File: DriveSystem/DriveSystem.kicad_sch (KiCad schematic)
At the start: 14 parts, among them SW1 SW_Push, SW2 SW_Push, SW3 SW_Push, SW4 SW_Push

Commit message: MC Custom Symbol
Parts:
- removed A1: Arduino_UNO_R2, Module:Arduino_UNO_R2, symbol MCU_Module:Arduino_UNO_R2
- removed RSP1: RSP-750-24, symbol CustomSymbols:RSP-750-24
- added J1: Raspberry_Pi_2_3, symbol Connector:Raspberry_Pi_2_3
- added U1: ~, symbol CustomSymbols:RoboClaw_2x30A_MC
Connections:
- new net: J1.1 (3V3), J1.17 (3V3)
- new net: J1.14 (GND), J1.20 (GND), J1.25 (GND), J1.30 (GND), J1.34 (GND), J1.39 (GND), J1.6 (GND), J1.9 (GND)
- new net: J1.2 (5V), J1.4 (5V)
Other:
- company: (none) -> TERRIER RIDE ENGINEERING CLUB
- title: (none) -> REC 2025 ELECTRONIC SCHEMATIC

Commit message: Merged RCP Schematic
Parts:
- removed C1, C2, C3, C4: 100n, symbol Device:C
- removed J1: Raspberry_Pi_2_3, symbol Connector:Raspberry_Pi_2_3
- removed R1, R2, R3, R4: 1k, symbol Device:R
- removed SW1, SW2, SW3, SW4: SW_Push, symbol Switch:SW_Push
- added Dispatch2, Restart2: SW_Push_LED, symbol Switch:SW_Push_LED
- added E-Stop2: SW_Push, symbol Switch:SW_Push_LED
- added F1: 1.5A Fuse, symbol Device:Fuse
- added F2: 30A Fuse, symbol Device:Fuse
- added J2: Raspberry_Pi_4, symbol Connector:Raspberry_Pi_4
- added K1: Fujitsu_FTR-LYAA005x, Relay_THT:Relay_SPST-NO_Fujitsu_FTR-LYAA005x_FormA_Vertical, symbol Relay:Fujitsu_FTR-LYAA005x
- added Ride off2: SW_Push_LED, symbol Switch:SW_Push_LED
- added U2: 5304 Gear Motor, symbol CustomSymbols:5304_Saturn_Gear_Motor
- added U3: 24VDC UBC-C PSU, symbol CustomSymbols:Pi_PSU
- U1: value ~ -> RoboClaw Motor Controller
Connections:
- net at U1. (5VDC): now also U2.6 (Ch_B)
- net at U1.1 (M1A): now also U2.2 (M+)
- net at U1.2 (M1B): now also U2.1 (M-)
- net at U1.3 (Vin+): now also K1.14
- net at U1.4 (Vin-): now also K1.A1, U3.2 (GND)
- net at U1.S1 (RX): now also J2.8 (GPIO14/UART_TXD)
- net at U1.S2 (TX): now also J2.10 (GPIO15/UART_RXD)
- new net: Dispatch2.2, E-Stop2.1, J2.1 (3V3), J2.15 (GPIO22/SDIO_CLK), J2.16 (GPIO23/SDIO_CMD), J2.17 (3V3), J2.18 (GPIO24/SDIO_DAT0), J2.22 (GPIO25/SDIO_DAT1), Restart2.2, Ride off2.2
- new net: Dispatch2.3 (K), J2.11 (GPIO17/SPI1_~{CE1})
- new net: Dispatch2.4 (A), J2.14 (GND), J2.20 (GND), J2.25 (GND), J2.30 (GND), J2.34 (GND), J2.39 (GND), J2.6 (GND), J2.9 (GND), Restart2.4 (A), Ride off2.4 (A)
- new net: U1. (5VDC), U2.3 (VCC)
- new net: U1. (5VDC), U2.4 (GND)
- new net: U1. (5VDC), U2.5 (Ch_A)
- new net: F1.1, U3.1 (+24VDC)
- new net: F1.2, F2.1, K1.13
- new net: J2. (USB-C_In), U3.3 (USB-C)
- new net: J2.12 (GPIO18/SPI1_~{CE0}/PCM_CLK/PWM0), Restart2.3 (K)
- new net: J2.2 (5V), J2.4 (5V)
- new net: J2.36 (GPIO16/SPI1_~{CE2}), Ride off2.3 (K)
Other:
- note added: "From RCC"
- note added: "Pin 1 represents NC Pin 2 represents NO Pin 3 represents (-)L2 light terminal Pin 4 represents (+)L2 light terminal"
- moved on the sheet: U1

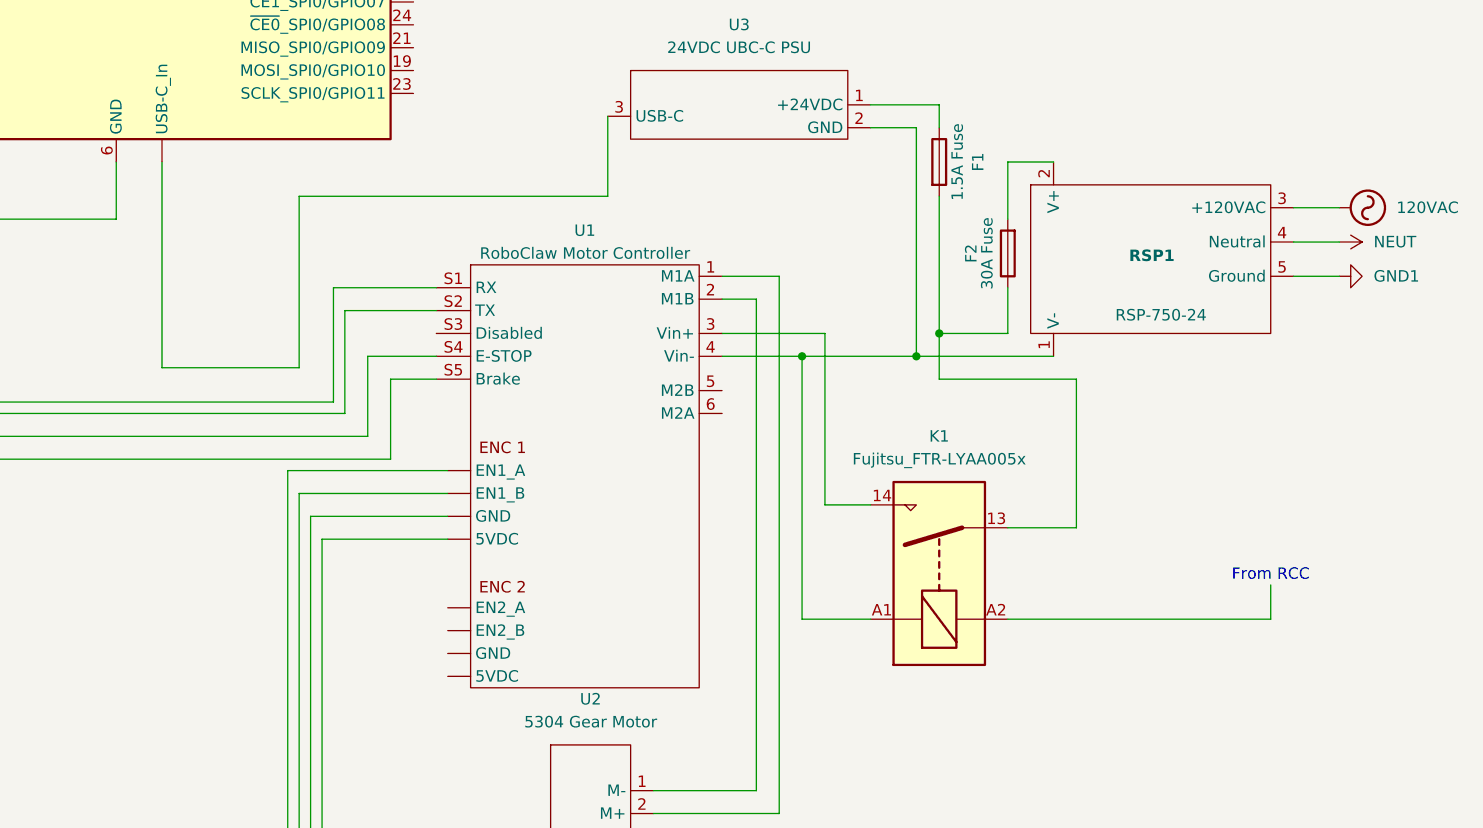
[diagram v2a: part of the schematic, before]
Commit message: Update DriveSystem.kicad_sch
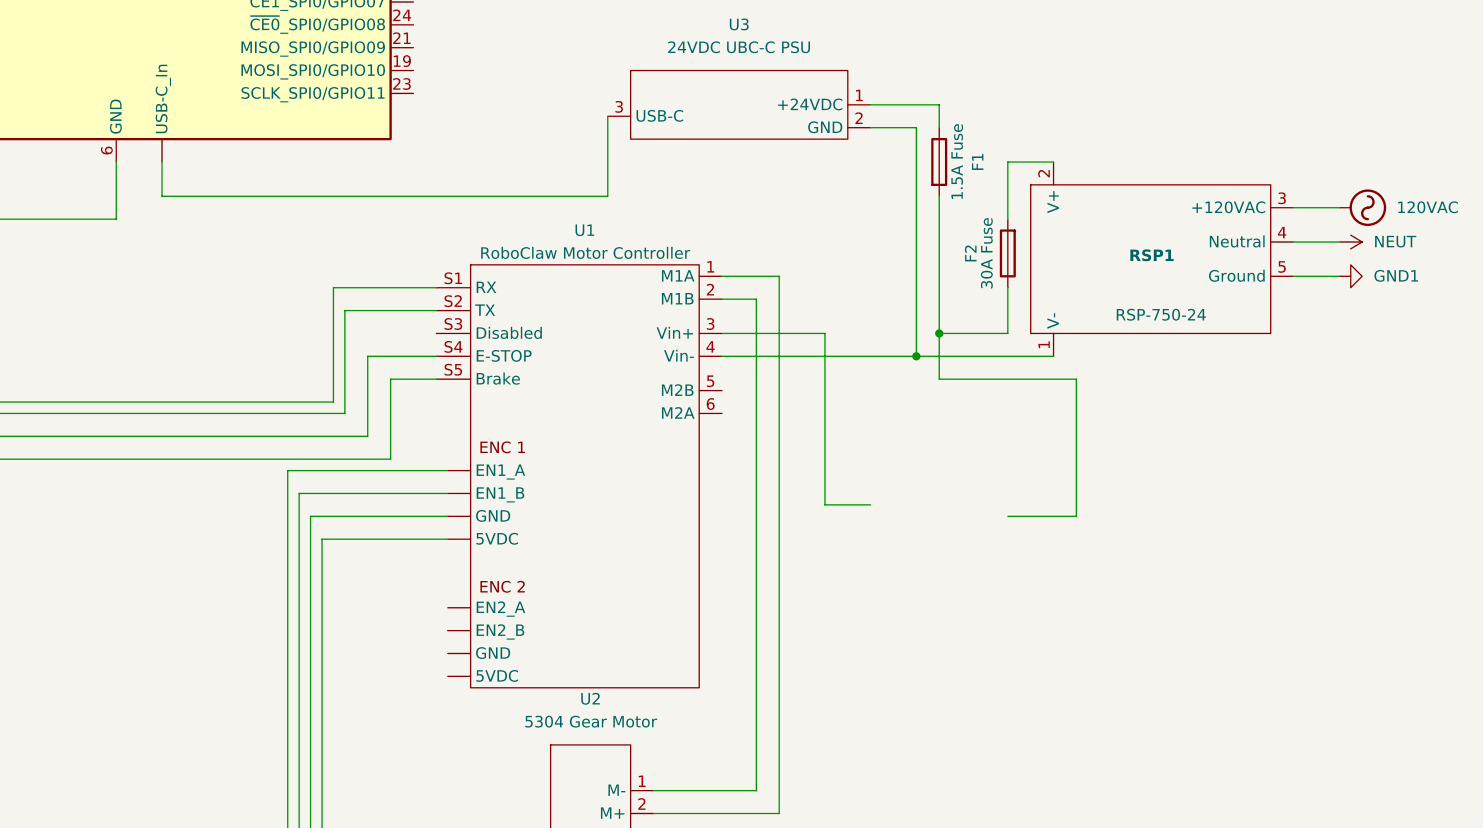
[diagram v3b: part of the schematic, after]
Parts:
- removed K1: Fujitsu_FTR-LYAA005x, Relay_THT:Relay_SPST-NO_Fujitsu_FTR-LYAA005x_FormA_Vertical, symbol Relay:Fujitsu_FTR-LYAA005x
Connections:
- net at U1. (5VDC): now also U2.6 (Ch_B)
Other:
- note removed: "From RCC"
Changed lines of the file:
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@@
-		)
-	)
-	(text "From RCC\n"
-		(exclude_from_sim no)
-		(at 243.84 136.144 0)
-		(effects
-			(font
-				(size 1.27 1.27)
-			)
 		)
 	)
@@
 	)
 	(junction
-		(at 191.77 111.76)
-		(diameter 0)
-		(color 0 0 0 0)
-	)
-	(junction
 		(at 46.99 48.26)
 		(diameter 0)
@@
 	(wire
 		(pts
-			(xy 222.25 114.3) (xy 222.25 130.81)
+			(xy 222.25 114.3) (xy 222.25 129.54)
 		)
 		(stroke
@@
 	(wire
 		(pts
-			(xy 120.65 113.03) (xy 135.89 113.03)
-		)
-		(stroke
-			(width 0)
-			(type default)
-		)
-	)
-	(wire
-		(pts
 			(xy 207.01 109.22) (xy 207.01 114.3)
 		)
@@
 	(wire
 		(pts
-			(xy 243.84 137.16) (xy 243.84 140.97)
-		)
-		(stroke
-			(width 0)
-			(type default)
-		)
-	)
-	(wire
-		(pts
 			(xy 170.18 93.98) (xy 170.18 85.09)
 		)
@@
 	(wire
 		(pts
-			(xy 191.77 140.97) (xy 191.77 111.76)
-		)
-		(stroke
-			(width 0)
-			(type default)
-		)
-	)
-	(wire
-		(pts
 			(xy 246.38 99.06) (xy 251.46 99.06)
 		)
@@
 	(wire
 		(pts
+			(xy 120.65 93.98) (xy 170.18 93.98)
+		)
+		(stroke
+			(width 0)
+			(type default)
+		)
+	)
+	(wire
+		(pts
 			(xy 49.53 49.53) (xy 49.53 48.26)
 		)
@@
 	(wire
 		(pts
-			(xy 135.89 93.98) (xy 135.89 113.03)
-		)
-		(stroke
-			(width 0)
-			(type default)
-		)
-	)
-	(wire
-		(pts
 			(xy 46.99 63.5) (xy 46.99 48.26)
 		)
@@
 	(wire
 		(pts
-			(xy 170.18 93.98) (xy 135.89 93.98)
-		)
-		(stroke
-			(width 0)
-			(type default)
-		)
-	)
-	(wire
-		(pts
 			(xy 43.18 93.98) (xy 67.31 93.98)
 		)
@@
 	(wire
 		(pts
-			(xy 120.65 113.03) (xy 120.65 90.17)
-		)
-		(stroke
-			(width 0)
-			(type default)
-		)
-	)
-	(wire
-		(pts
 			(xy 40.64 45.72) (xy 53.34 45.72)
 		)
@@
 	(wire
 		(pts
-			(xy 191.77 111.76) (xy 204.47 111.76)
+			(xy 182.88 111.76) (xy 204.47 111.76)
 		)
 		(stroke
@@
 	(wire
 		(pts
-			(xy 243.84 140.97) (xy 214.63 140.97)
-		)
-		(stroke
-			(width 0)
-			(type default)
-		)
-	)
-	(wire
-		(pts
 			(xy 40.64 25.4) (xy 165.1 25.4)
 		)
@@
 	(wire
 		(pts
-			(xy 199.39 140.97) (xy 191.77 140.97)
-		)
-		(stroke
-			(width 0)
-			(type default)
-		)
-	)
-	(wire
-		(pts
 			(xy 43.18 93.98) (xy 43.18 96.52)
 		)
@@
 	(wire
 		(pts
-			(xy 222.25 130.81) (xy 214.63 130.81)
+			(xy 222.25 129.54) (xy 214.63 129.54)
 		)
 		(stroke
@@
 	(wire
 		(pts
+			(xy 120.65 93.98) (xy 120.65 90.17)
+		)
+		(stroke
+			(width 0)
+			(type default)
+		)
+	)
+	(wire
+		(pts
 			(xy 40.64 60.96) (xy 58.42 60.96)
 		)
@@
 			(type default)
 			(color 165 65 154 1)
-		)
-	)
-	(wire
-		(pts
-			(xy 182.88 111.76) (xy 191.77 111.76)
-		)
-		(stroke
-			(width 0)
-			(type default)
 		)
 	)
@@
 					(unit 1)
 				)
-			)
-		)
-	)
-	(symbol
-		(lib_id "Relay:Fujitsu_FTR-LYAA005x")
-		(at 207.01 135.89 90)
-		(unit 1)
-		(exclude_from_sim no)
-		(in_bom yes)
-		(on_board yes)
-		(dnp no)
-		(fields_autoplaced yes)
-		(property "Reference" "K1"
-			(at 207.01 120.65 90)
-			(effects
-				(font
-					(size 1.27 1.27)
-				)
-			)
-		)
-		(property "Value" "Fujitsu_FTR-LYAA005x"
-			(at 207.01 123.19 90)
-			(effects
-				(font
-					(size 1.27 1.27)
-				)
-			)
-		)
-		(property "Footprint" "Relay_THT:Relay_SPST-NO_Fujitsu_FTR-LYAA005x_FormA_Vertical"
-			(at 208.28 124.46 0)
-			(effects
-				(font
-					(size 1.27 1.27)
-				)
-				(justify left)
-				(hide yes)
-			)
-		)
-		(property "Datasheet" "https://www.fujitsu.com/sg/imagesgig5/ftr-ly.pdf"
-			(at 210.82 118.11 0)
-			(effects
-				(font
-					(size 1.27 1.27)
-				)
-				(justify left)
-				(hide yes)
-			)
-		)
-		(property "Description" "Relay, SPST Form A, vertical mount, 5-60V coil, 6A, 250VAC, 28 x 5 x 15mm"
-			(at 207.01 135.89 0)
-			(effects
-				(font
-					(size 1.27 1.27)
-				)
-				(hide yes)
-			)
-		)
-		(pin "14"
-		)
-		(pin "A1"
-		)
-		(pin "13"
-		)
-		(pin "A2"
-		)
-		(instances
-			(project ""
-				(path "/09f307af-601f-4645-b594-daaafb49fd2a"
-					(reference "K1")
-					(unit 1)
-				)
